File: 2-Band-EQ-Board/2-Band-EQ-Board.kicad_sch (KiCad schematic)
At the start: 18 parts, among them J1 Conn_02x03_Odd_Even, U1 TL072

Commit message: Final version 1.0 ordered
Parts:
- C1: value 100n -> 33n
- C11, C9: value 3.3u -> 1.5u
- C2: value 3.3u -> 0.68u
- C3: value 56n -> 15n
- C4: value 1.5u -> 0.33u
- J1: value Conn_02x03_Odd_Even -> PHED-DS006G1ABOGA-A006
- U1: value TL072 -> 296-TL072HIDRCT-ND
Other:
- title: (none) -> 2-Band-Gyrator
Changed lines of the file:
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@@
 	(generator_version "8.0")
 	(paper "A4")
+	(title_block
+		(title "2-Band-Gyrator")
+		(date "2024-11-23")
+		(rev "1.0")
+	)
 	(junction
 		(at 116.84 111.76)
@@
 			)
 		)
-		(property "Value" "100n"
+		(property "Value" "33n"
 			(at 146.05 101.6492 90)
 			(effects
@@
 			)
 		)
-		(property "Description" ""
+		(property "Description" "CC0603JRX7R9BB333"
 			(at 146.05 105.41 0)
 			(effects
@@
 			)
 		)
-		(property "Value" "TL072"
+		(property "Value" "296-TL072HIDRCT-ND"
 			(at 92.075 112.8537 0)
 			(effects
@@
 			)
 		)
-		(property "Datasheet" "http://www.ti.com/lit/ds/symlink/tl071.pdf"
+		(property "Datasheet" "https://www.digikey.com/en/products/detail/texas-instruments/TL072HIDR/15205173"
 			(at 93.98 111.76 0)
 			(effects
@@
 			)
 		)
-		(property "Value" "1.5u"
+		(property "Value" "0.33u"
 			(at 203.581 96.3437 0)
 			(effects
@@
 			)
 		)
-		(property "Datasheet" ""
+		(property "Datasheet" "https://www.digikey.com/en/products/detail/samsung-electro-mechanics/CL31B335KAHVPNE/5961344"
 			(at 200.66 95.25 0)
 			(effects
@@
 			)
 		)
-		(property "Value" "TL072"
+		(property "Value" "296-TL072HIDRCT-ND"
 			(at 200.66 127.3318 0)
 			(effects
@@
 			)
 		)
-		(property "Datasheet" "http://www.ti.com/lit/ds/symlink/tl071.pdf"
+		(property "Datasheet" "https://www.digikey.com/en/products/detail/texas-instruments/TL072HIDR/15205173"
 			(at 200.66 120.65 0)
 			(effects
@@
 			)
 		)
-		(property "Value" "56n"
+		(property "Value" "15n"
 			(at 191.77 101.6492 90)
 			(effects
@@
 			)
 		)
-		(property "Description" ""
+		(property "Description" "CC0603JRX7R9BB153"
 			(at 191.77 105.41 0)
 			(effects
@@
 			)
 		)
-		(property "Value" "Conn_02x03_Odd_Even"
+		(property "Value" "PHED-DS006G1ABOGA-A006"
 			(at 151.13 148.2582 0)
 			(effects
@@
 			)
 		)
-		(property "Datasheet" "~"
+		(property "Datasheet" "https://www.digikey.com/en/products/detail/superior-tech/PHED-DS006G1ABOGA-A006/16583466"
 			(at 149.86 153.67 0)
 			(effects
@@
 			)
 		)
-		(property "Description" "Generic connector, double row, 02x03, odd/even pin numbering scheme (row 1 odd numbers, row 2 even numbers), script generated (kicad-library-utils/schlib/autogen/connector/)"
+		(property "Description" "MALE HEADER VERTICAL THROUGH HOL"
 			(at 149.86 153.67 0)
 			(effects
@@
 			)
 		)
-		(property "Datasheet" "~"
+		(property "Datasheet" "https://www.digikey.com/en/products/detail/kemet/ESK107M016AC3AA/3083016"
 			(at 106.68 118.11 0)
 			(effects
@@
 			)
 		)
-		(property "Description" "Polarized capacitor"
+		(property "Description" "CAP ALUM 100UF 20% 16V RADIAL TH"
 			(at 106.68 118.11 0)
 			(effects
@@
 			)
 		)
-		(property "Value" "3.3u"
+		(property "Value" "0.68u"
 			(at 157.861 96.3437 0)
 			(effects
@@
 			)
 		)
-		(property "Datasheet" ""
+		(property "Datasheet" "https://www.digikey.com/en/products/detail/yageo/CC0603KRX7R8BB684/16797741"
 			(at 154.94 95.25 0)
 			(effects
@@
 			)
 		)
-		(property "Value" "3.3u"
+		(property "Value" "1.5u"
 			(at 168.021 96.3437 0)
 			(effects
@@
 			)
 		)
-		(property "Datasheet" "~"
+		(property "Datasheet" "https://www.digikey.com/en/products/detail/kemet/ESK107M016AC3AA/3083016"
 			(at 106.68 105.41 0)
 			(effects
@@
 			)
 		)
-		(property "Description" "Polarized capacitor"
+		(property "Description" "CAP ALUM 100UF 20% 16V RADIAL TH"
 			(at 106.68 105.41 0)
 			(effects
@@
 			)
 		)
-		(property "Value" "3.3u"
+		(property "Value" "1.5u"
 			(at 213.741 96.3437 0)
 			(effects
@@
 			)
 		)
-		(property "Value" "TL072"
+		(property "Value" "296-TL072HIDRCT-ND"
 			(at 154.94 127.3318 0)
 			(effects
@@
 			)
 		)
-		(property "Datasheet" "http://www.ti.com/lit/ds/symlink/tl071.pdf"
+		(property "Datasheet" "https://www.digikey.com/en/products/detail/texas-instruments/TL072HIDR/15205173"
 			(at 154.94 120.65 0)
 			(effects

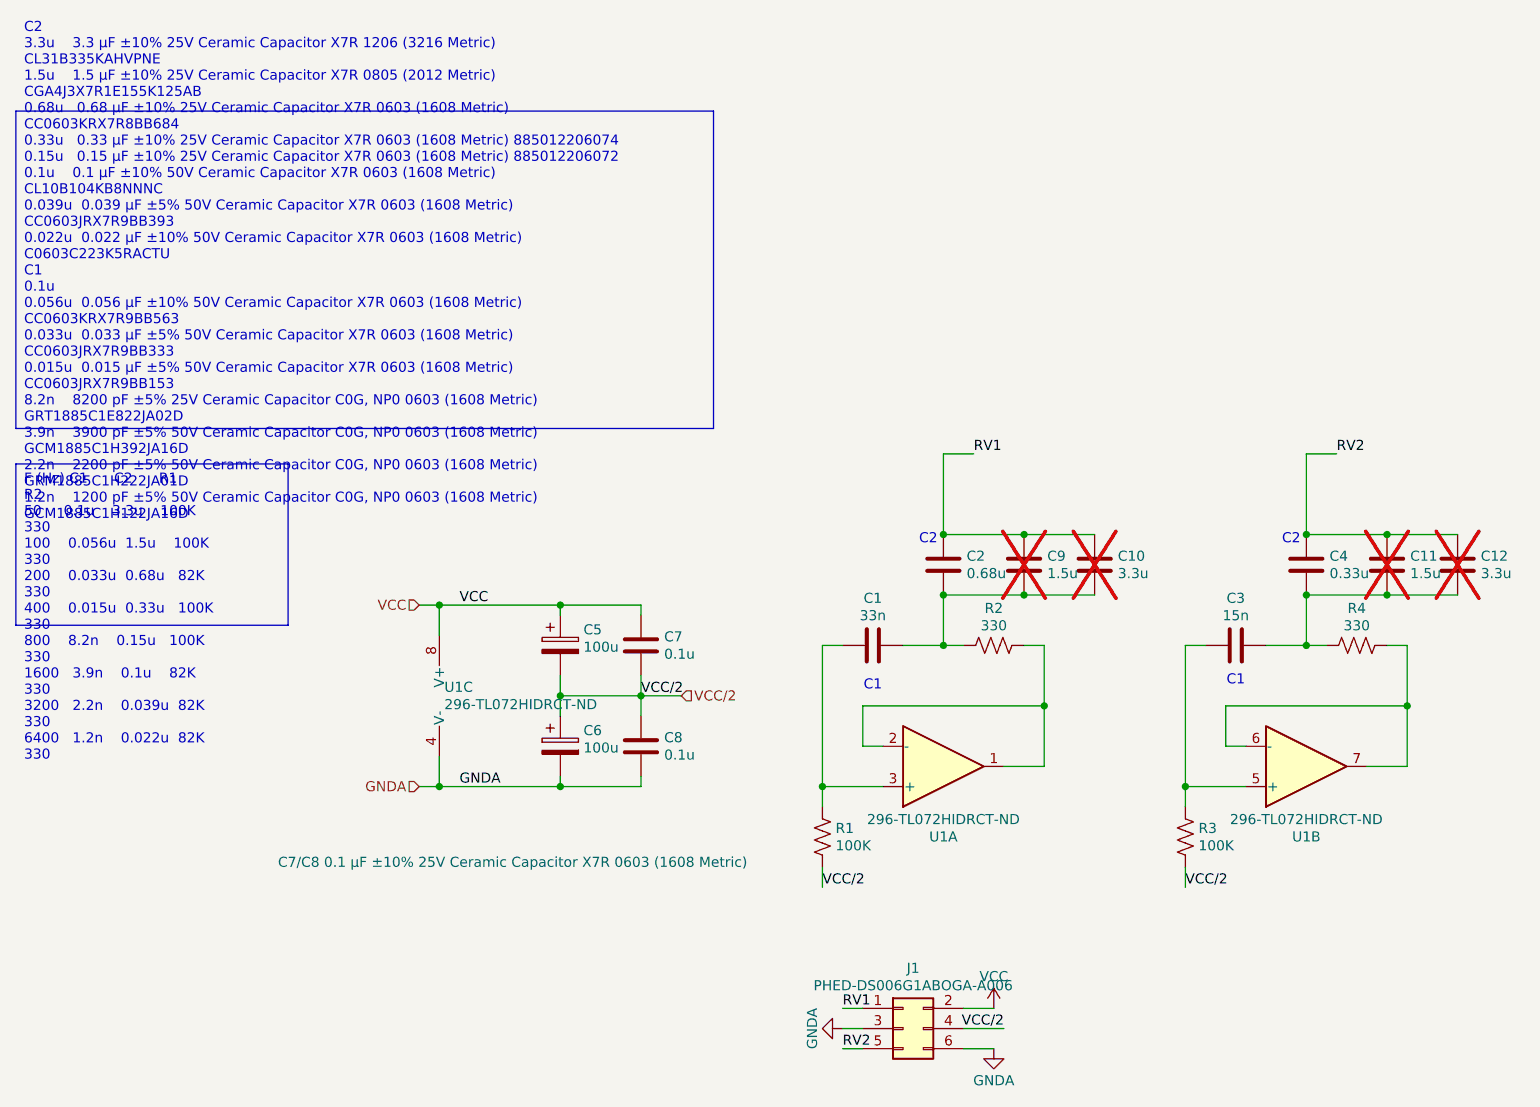
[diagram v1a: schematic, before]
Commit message: Fix bypass resistor, add missing Vcc. Move to Kicad-9
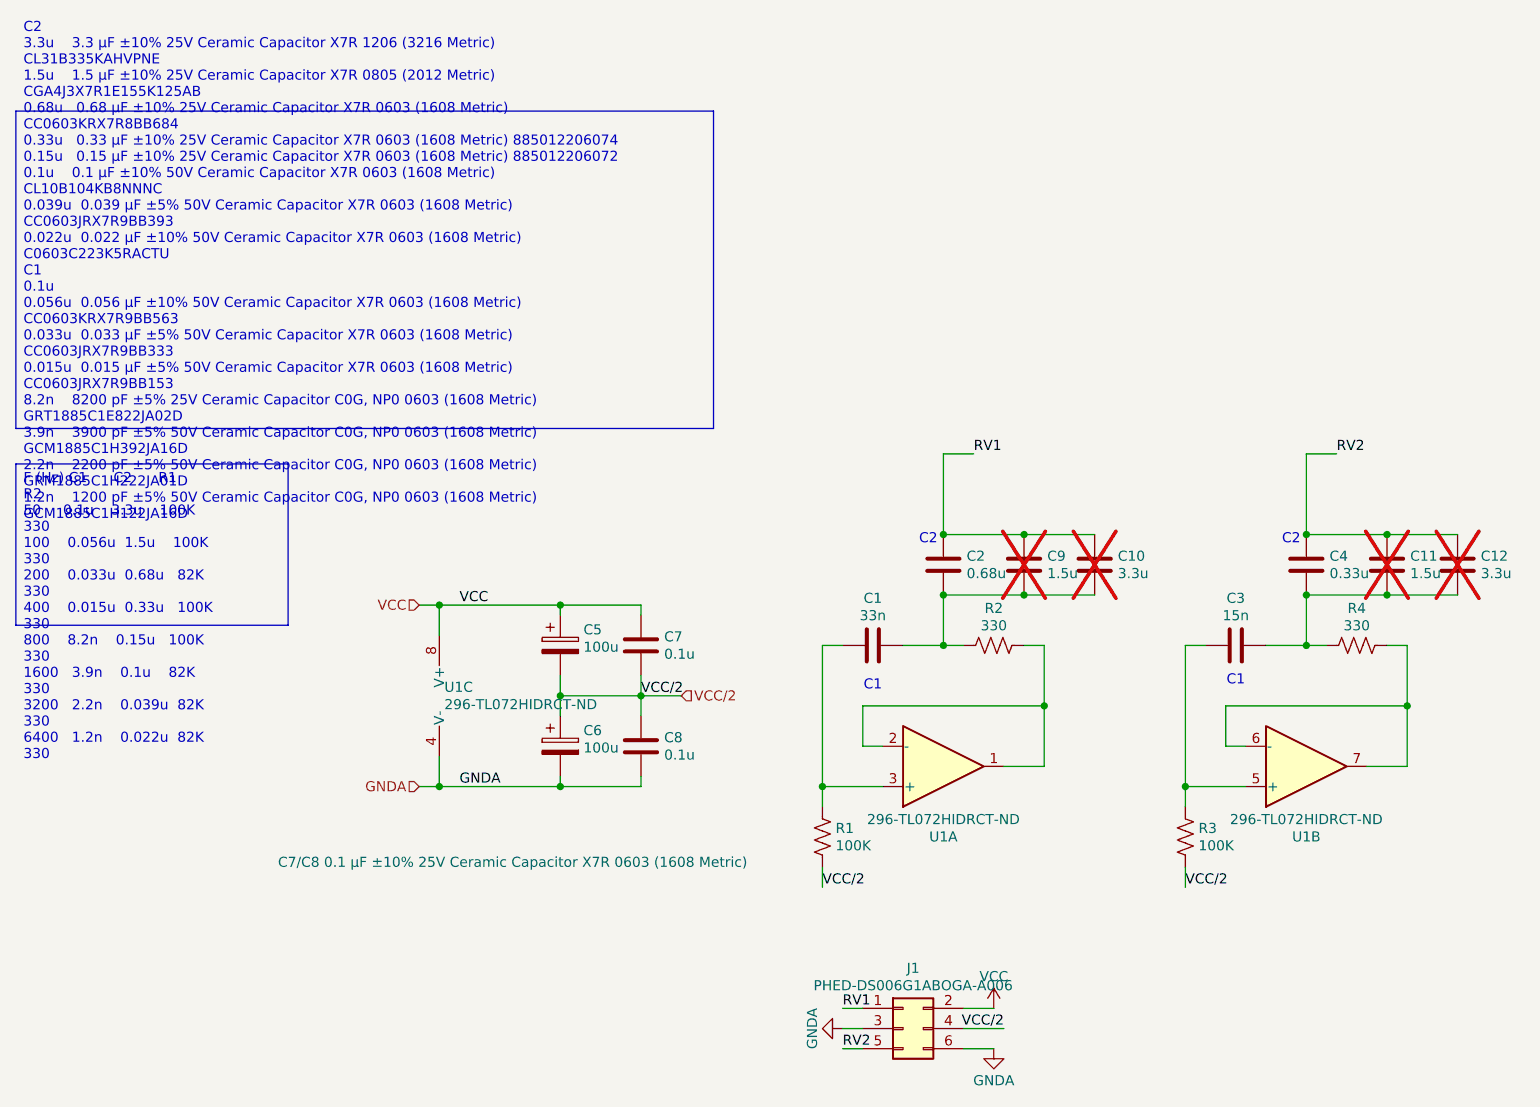
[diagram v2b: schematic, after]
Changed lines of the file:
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@@
 (kicad_sch
-	(version 20231120)
+	(version 20250114)
 	(generator "eeschema")
-	(generator_version "8.0")
-	(paper "A4")
+	(generator_version "9.0")
+	(paper "USLetter")
 	(title_block
 		(title "2-Band-Gyrator")
@@
 		(rev "1.0")
 	)
+	(text "C1"
+		(exclude_from_sim no)
+		(at 191.77 109.855 0)
+		(effects
+			(font
+				(size 1.27 1.27)
+			)
+		)
+	)
+	(text "C2"
+		(exclude_from_sim no)
+		(at 198.755 92.075 0)
+		(effects
+			(font
+				(size 1.27 1.27)
+			)
+		)
+	)
+	(text "C1"
+		(exclude_from_sim no)
+		(at 146.05 110.49 0)
+		(effects
+			(font
+				(size 1.27 1.27)
+			)
+		)
+	)
+	(text "C2"
+		(exclude_from_sim no)
+		(at 153.035 92.075 0)
+		(effects
+			(font
+				(size 1.27 1.27)
+			)
+		)
+	)
+	(text_box "C2    \n3.3u    3.3 µF ±10% 25V Ceramic Capacitor X7R 1206 (3216 Metric) CL31B335KAHVPNE\n1.5u    1.5 µF ±10% 25V Ceramic Capacitor X7R 0805 (2012 Metric) CGA4J3X7R1E155K125AB\n0.68u   0.68 µF ±10% 25V Ceramic Capacitor X7R 0603 (1608 Metric) CC0603KRX7R8BB684\n0.33u   0.33 µF ±10% 25V Ceramic Capacitor X7R 0603 (1608 Metric) 885012206074\n0.15u   0.15 µF ±10% 25V Ceramic Capacitor X7R 0603 (1608 Metric) 885012206072\n0.1u    0.1 µF ±10% 50V Ceramic Capacitor X7R 0603 (1608 Metric) CL10B104KB8NNNC\n0.039u  0.039 µF ±5% 50V Ceramic Capacitor X7R 0603 (1608 Metric) CC0603JRX7R9BB393\n0.022u  0.022 µF ±10% 50V Ceramic Capacitor X7R 0603 (1608 Metric) C0603C223K5RACTU\nC1    \n0.1u    \n0.056u  0.056 µF ±10% 50V Ceramic Capacitor X7R 0603 (1608 Metric) CC0603KRX7R9BB563\n0.033u  0.033 µF ±5% 50V Ceramic Capacitor X7R 0603 (1608 Metric) CC0603JRX7R9BB333\n0.015u  0.015 µF ±5% 50V Ceramic Capacitor X7R 0603 (1608 Metric) CC0603JRX7R9BB153\n8.2n    8200 pF ±5% 25V Ceramic Capacitor C0G, NP0 0603 (1608 Metric) GRT1885C1E822JA02D\n3.9n    3900 pF ±5% 50V Ceramic Capacitor C0G, NP0 0603 (1608 Metric) GCM1885C1H392JA16D\n2.2n    2200 pF ±5% 50V Ceramic Capacitor C0G, NP0 0603 (1608 Metric) GRM1885C1H222JA01D\n1.2n    1200 pF ±5% 50V Ceramic Capacitor C0G, NP0 0603 (1608 Metric) GCM1885C1H122JA16D"
+		(exclude_from_sim no)
+		(at 38.1 38.1 0)
+		(size 87.8822 39.9827)
+		(margins 0.9525 0.9525 0.9525 0.9525)
+		(stroke
+			(width 0)
+			(type default)
+		)
+		(fill
+			(type none)
+		)
+		(effects
+			(font
+				(size 1.27 1.27)
+			)
+			(justify left)
+		)
+	)
+	(text_box "F (Hz) C1      C2      R1     R2\n50     0.1u    3.3u    100K   330\n100    0.056u  1.5u    100K   330\n200    0.033u  0.68u   82K    330\n400    0.015u  0.33u   100K   330\n800    8.2n    0.15u   100K   330\n1600   3.9n    0.1u    82K    330\n3200   2.2n    0.039u  82K    330\n6400   1.2n    0.022u  82K    330"
+		(exclude_from_sim no)
+		(at 38.1 82.55 0)
+		(size 34.29 20.32)
+		(margins 0.9525 0.9525 0.9525 0.9525)
+		(stroke
+			(width 0)
+			(type default)
+		)
+		(fill
+			(type none)
+		)
+		(effects
+			(font
+				(size 1.27 1.27)
+			)
+			(justify left top)
+		)
+	)
 	(junction
 		(at 116.84 111.76)
@@
 		)
 	)
-	(text_box "C2    \n3.3u    3.3 µF ±10% 25V Ceramic Capacitor X7R 1206 (3216 Metric) CL31B335KAHVPNE\n1.5u    1.5 µF ±10% 25V Ceramic Capacitor X7R 0805 (2012 Metric) CGA4J3X7R1E155K125AB\n0.68u   0.68 µF ±10% 25V Ceramic Capacitor X7R 0603 (1608 Metric) CC0603KRX7R8BB684\n0.33u   0.33 µF ±10% 25V Ceramic Capacitor X7R 0603 (1608 Metric) 885012206074\n0.15u   0.15 µF ±10% 25V Ceramic Capacitor X7R 0603 (1608 Metric) 885012206072\n0.1u    0.1 µF ±10% 50V Ceramic Capacitor X7R 0603 (1608 Metric) CL10B104KB8NNNC\n0.039u  0.039 µF ±5% 50V Ceramic Capacitor X7R 0603 (1608 Metric) CC0603JRX7R9BB393\n0.022u  0.022 µF ±10% 50V Ceramic Capacitor X7R 0603 (1608 Metric) C0603C223K5RACTU\nC1    \n0.1u    \n0.056u  0.056 µF ±10% 50V Ceramic Capacitor X7R 0603 (1608 Metric) CC0603KRX7R9BB563\n0.033u  0.033 µF ±5% 50V Ceramic Capacitor X7R 0603 (1608 Metric) CC0603JRX7R9BB333\n0.015u  0.015 µF ±5% 50V Ceramic Capacitor X7R 0603 (1608 Metric) CC0603JRX7R9BB153\n8.2n    8200 pF ±5% 25V Ceramic Capacitor C0G, NP0 0603 (1608 Metric) GRT1885C1E822JA02D\n3.9n    3900 pF ±5% 50V Ceramic Capacitor C0G, NP0 0603 (1608 Metric) GCM1885C1H392JA16D\n2.2n    2200 pF ±5% 50V Ceramic Capacitor C0G, NP0 0603 (1608 Metric) GRM1885C1H222JA01D\n1.2n    1200 pF ±5% 50V Ceramic Capacitor C0G, NP0 0603 (1608 Metric) GCM1885C1H122JA16D"
-		(exclude_from_sim no)
-		(at 38.1 38.1 0)
-		(size 87.8822 39.9827)
-		(stroke
-			(width 0)
-			(type default)
-		)
-		(fill
-			(type none)
-		)
+	(label "VCC{slash}2"
+		(at 139.7 135.89 0)
 		(effects
 			(font
 				(size 1.27 1.27)
 			)
-			(justify left)
-		)
-	)
-	(text_box "F (Hz) C1      C2      R1     R2\n50     0.1u    3.3u    100K   330\n100    0.056u  1.5u    100K   330\n200    0.033u  0.68u   82K    330\n400    0.015u  0.33u   100K   330\n800    8.2n    0.15u   100K   330\n1600   3.9n    0.1u    82K    330\n3200   2.2n    0.039u  82K    330\n6400   1.2n    0.022u  82K    330"
-		(exclude_from_sim no)
-		(at 38.1 82.55 0)
-		(size 34.29 20.32)
-		(stroke
-			(width 0)
-			(type default)
-		)
-		(fill
-			(type none)
-		)
+			(justify left bottom)
+		)
+	)
+	(label "GNDA"
+		(at 93.98 123.19 0)
 		(effects
 			(font
 				(size 1.27 1.27)
 			)
-			(justify left top)
-		)
-	)
-	(text "C1"
-		(exclude_from_sim no)
-		(at 191.77 109.855 0)
+			(justify left bottom)
+		)
+	)
+	(label "RV1"
+		(at 158.75 81.28 0)
 		(effects
 			(font
 				(size 1.27 1.27)
 			)
-		)
-	)
-	(text "C2"
-		(exclude_from_sim no)
-		(at 198.755 92.075 0)
+			(justify left bottom)
+		)
+	)
+	(label "VCC{slash}2"
+		(at 185.42 135.89 0)
 		(effects
 			(font
 				(size 1.27 1.27)
 			)
-		)
-	)
-	(text "C1"
-		(exclude_from_sim no)
-		(at 146.05 110.49 0)
+			(justify left bottom)
+		)
+	)
+	(label "VCC"
+		(at 93.98 100.33 0)
 		(effects
 			(font
 				(size 1.27 1.27)
 			)
-		)
-	)
-	(text "C2"
-		(exclude_from_sim no)
-		(at 153.035 92.075 0)
+			(justify left bottom)
+		)
+	)
+	(label "VCC{slash}2"
+		(at 162.56 153.67 180)
 		(effects
 			(font
 				(size 1.27 1.27)
 			)
+			(justify right bottom)
 		)
 	)
 	(label "VCC{slash}2"
-		(at 139.7 135.89 0)
-		(fields_autoplaced yes)
+		(at 116.84 111.76 0)
 		(effects
 			(font
@@
 		)
 	)
-	(label "GNDA"
-		(at 93.98 123.19 0)
-		(fields_autoplaced yes)
+	(label "RV1"
+		(at 142.24 151.13 0)
 		(effects
 			(font
@@
 		)
 	)
-	(label "RV1"
-		(at 158.75 81.28 0)
-		(fields_autoplaced yes)
+	(label "RV2"
+		(at 142.24 156.21 0)
 		(effects
 			(font
@@
 		)
 	)
-	(label "VCC{slash}2"
-		(at 185.42 135.89 0)
-		(fields_autoplaced yes)
+	(label "RV2"
+		(at 204.47 81.28 0)
 		(effects
 			(font
@@
 		)
 	)
-	(label "VCC"
-		(at 93.98 100.33 0)
-		(fields_autoplaced yes)
+	(hierarchical_label "GNDA"
+		(shape input)
+		(at 88.9 123.19 180)
 		(effects
 			(font
 				(size 1.27 1.27)
 			)
-			(justify left bottom)
-		)
-	)
-	(label "VCC{slash}2"
-		(at 162.56 153.67 180)
-		(fields_autoplaced yes)
+			(justify right)
+		)
+	)
+	(hierarchical_label "VCC{slash}2"
+		(shape input)
+		(at 121.92 111.76 0)
 		(effects
 			(font
 				(size 1.27 1.27)
 			)
-			(justify right bottom)
-		)
-	)
-	(label "VCC{slash}2"
-		(at 116.84 111.76 0)
-		(fields_autoplaced yes)
-		(effects
-			(font
-				(size 1.27 1.27)
-			)
-			(justify left bottom)
-		)
-	)
-	(label "RV1"
-		(at 142.24 151.13 0)
-		(fields_autoplaced yes)
-		(effects
-			(font
-				(size 1.27 1.27)
-			)
-			(justify left bottom)
-		)
-	)
-	(label "RV2"
-		(at 142.24 156.21 0)
-		(fields_autoplaced yes)
-		(effects
-			(font
-				(size 1.27 1.27)
-			)
-			(justify left bottom)
-		)
-	)
-	(label "RV2"
-		(at 204.47 81.28 0)
-		(fields_autoplaced yes)
-		(effects
-			(font
-				(size 1.27 1.27)
-			)
-			(justify left bottom)
-		)
-	)
-	(hierarchical_label "GNDA"
-		(shape input)
-		(at 88.9 123.19 180)
-		(fields_autoplaced yes)
-		(effects
-			(font
-				(size 1.27 1.27)
-			)
-			(justify right)
-		)
-	)
-	(hierarchical_label "VCC{slash}2"
-		(shape input)
-		(at 121.92 111.76 0)
-		(fields_autoplaced yes)
-		(effects
-			(font
-				(size 1.27 1.27)
-			)
 			(justify left)
 		)
@@
 		(shape input)
 		(at 88.9 100.33 180)
-		(fields_autoplaced yes)
 		(effects
 			(font
@@
 		)
 	)
+	(embedded_fonts no)
 )
